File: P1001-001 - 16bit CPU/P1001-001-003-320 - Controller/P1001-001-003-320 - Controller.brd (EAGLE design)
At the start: 200 x 152 mm, 129 parts, among them IC10 74ALS00D, IC21 74LS138D, IC22 74LS138D, IC27 MEGA8535-A, IC3 74LS138D, IC4 74LS138D, IC5 74LS138D, J1 22-27-2041-04

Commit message: Check in the first try at soldering up the board
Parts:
- removed ABC_CLEAR, HALT_RESEDT_NEXTINS, PC_MAR_IR_IN, RAM_STACK_IN: (no value), jumper:JP2W
- removed B_OUT_PIMS, IN_C_D_X, STACK_C, STEP_PINS: (no value), jumper:JP4
- removed EXTRA6, INTERUPT_OUT: (no value), led:SFH482
- removed EXTRA_1_2_PINS, EXTRA_3_4_PINS, EXTRA_5_6_PINS, INTERUPTS, PC_INC_DEC, RAM_IMT_OUT: (no value), jumper:JP1
- removed IC10: 74ALS00D, 74xx-us:SO14
- removed J1: 22-27-2041-04, con-molex:6410-04
- removed PULL_DOWN: (no value), rcl:M0805
- removed R10: (no value), resistor-bourns:SO16
- added A11_A8, A15_A12, A7_A5, B11_B8, B15_B12, B7_B6, B_OUT_PINS, C11_C8, C15_C12, C7-C4, RAM_OUT_INTER: (no value), jumper:JP4
- added ALU_OUT, C_CLEAR_LED, FLAG_IN, INTER_DIS, INTER_EN, INTR_FLAG_OUT, INTR_REG_OUT: (no value), led:SFH482
- added IC1: 74ALS00D, 74xx-us:SO14
- added IC2: 74ALS02D, 74xx-us:SO14
- added IC6: 74ALS08D, 74xx-us:SO14
- added R6: (no value), resistor-bourns:SO16
- added STEP1_STEP3: (no value), jumper:JP2
- added STEP9: (no value), jumper:JP1
- moved PAUSE_INERUPT 102.0 mm to (133.0, 59.0)
- moved PLAY_INTERUPT 96.0 mm to (121.0, 59.0)
- moved X_OUT 83.2 mm to (13.0, 24.0)
- moved HALT 78.4 mm to (170.0, 60.0)
- moved EXTRA1 75.7 mm to (115.0, 48.0)
- moved EXTRA2 75.7 mm to (121.0, 48.0)
- moved EXTRA3 75.7 mm to (127.0, 48.0)
- moved EXTRA4 75.7 mm to (133.0, 48.0)
- moved EXTRA5 75.7 mm to (139.0, 48.0)
- moved RAM_OUT 74.6 mm to (41.0, 24.0)
- moved C_OUT 73.8 mm to (14.0, 36.0)
- moved NEXT_INS 72.7 mm to (158.0, 60.0)
- moved D_CLEAR_LED 69.6 mm to (77.0, 36.0)
- moved C_DEC 67.7 mm to (20.0, 36.0)
- moved C_INC 67.7 mm to (26.0, 36.0)
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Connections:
- new net FIRST_STEP: IC6.3, STEP9.1
- new net N$42: EXTRA5.K, R5.3
- new net N$50: EXTRA_OUT.3, EXTRA_OUT3.K, IC5.9
- new net N$56: EXTRA_OUT.4, EXTRA_OUT4.K, IC5.7
- new net N$57: EXTRA_OUT3.A, R2.9
- new net N$58: EXTRA_OUT4.A, R2.10
- new net N$59: R5.8, RESET.K
- new net N$60: HALT.K, R5.7
- new net N$61: IC2.4, IC6.2
- new net N$62: IC2.1, IC6.1
- new net N$63: NEXT_INS.K, R5.6
- net !CLEAR: now also IC1.1, IC1.2, IC1.6; no longer IC10.1, IC10.2, IC10.6
- net CLEAR: now also IC1.3; no longer IC10.3
- net DATAA10: now also A11_A8.3, A_CLEAR_LED.K; no longer EXTRA6.K, EXTRA_5_6_PINS.2
- net DATAA11: now also A11_A8.4, B_CLEAR_LED.K; no longer ABC_CLEAR.1, A_CLEAR_LED.K
- net DATAA12: now also A15_A12.1, C_CLEAR_LED.K; no longer ABC_CLEAR.2, B_CLEAR_LED.K
- net DATAA13: now also A15_A12.2; no longer ABC_CLEAR.3
- net DATAA14: now also A15_A12.3; no longer INTERUPTS.1
- net DATAA15: now also A15_A12.4; no longer INTERUPTS.2
- net DATAA5: now also A7_A5.2; no longer EXTRA_1_2_PINS.1
- net DATAA6: now also A7_A5.3; no longer EXTRA_1_2_PINS.2
- net DATAA7: now also A7_A5.4; no longer EXTRA_3_4_PINS.1
- net DATAA8: now also A11_A8.1; no longer EXTRA_3_4_PINS.2
- net DATAA9: now also A11_A8.2, EXTRA5.A; no longer EXTRA5.K, EXTRA_5_6_PINS.1
- net DATAB10: now also B11_B8.3; no longer PC_MAR_IR_IN.1
- net DATAB11: now also B11_B8.4; no longer PC_MAR_IR_IN.2
- net DATAB12: now also B15_B12.1; no longer PC_MAR_IR_IN.3
- net DATAB13: now also B15_B12.2; no longer RAM_STACK_IN.1
- net DATAB14: now also B15_B12.3; no longer RAM_STACK_IN.2
- net DATAB15: now also B15_B12.4; no longer RAM_STACK_IN.3
- net DATAB4: no longer PC_INC_DEC.2
- net DATAB6: now also B7_B6.3; no longer IN_C_D_X.1
- net DATAB7: now also B7_B6.4; no longer IN_C_D_X.2
- net DATAB8: now also B11_B8.1; no longer IN_C_D_X.3
- net DATAB9: now also B11_B8.2; no longer IN_C_D_X.4
- net DATAC10: now also C11_C8.3, FLAG_IN.A
- net DATAC11: now also C11_C8.4, INTER_EN.A
- net DATAC12: now also C15_C12.1, INTER_DIS.A
- net DATAC13: now also C15_C12.2, RESET.A; no longer HALT_RESEDT_NEXTINS.3, RESET.K
- net DATAC14: now also C15_C12.3, HALT.A; no longer HALT.K, HALT_RESEDT_NEXTINS.2
- net DATAC15: now also C15_C12.4, NEXT_INS.A; no longer HALT_RESEDT_NEXTINS.1, NEXT_INS.K
- net DATAC4: now also C7-C4.1, PC_DEC.A; no longer PC_DEC.K
- net DATAC5: now also C7-C4.2, PC_INC.A; no longer PC_INC.K, PC_INC_DEC.1
- net DATAC6: now also C7-C4.3, STACK_INC.A; no longer STACK_C.4, STACK_INC.K
- net DATAC7: now also C7-C4.4, STACK_DEC.A; no longer STACK_C.3, STACK_DEC.K
- net DATAC8: now also C11_C8.1, C_INC.A; no longer C_INC.K, STACK_C.2
- net DATAC9: now also C11_C8.2, C_DEC.A; no longer C_DEC.K, STACK_C.1
- net EXTERN_BUS0: no longer R10.1
- net EXTERN_BUS1: no longer R10.9
- net EXTERN_BUS10: no longer R10.6
- net EXTERN_BUS11: no longer R10.14
- net EXTERN_BUS12: no longer R10.7
- net EXTERN_BUS13: no longer R10.15
- net EXTERN_BUS14: no longer R10.8
- net EXTERN_BUS15: no longer PULL_DOWN.1
- net EXTERN_BUS2: no longer R10.2
- net EXTERN_BUS3: no longer R10.10
- net EXTERN_BUS4: no longer R10.3
- net EXTERN_BUS5: no longer R10.11
- net EXTERN_BUS6: no longer R10.4
- net EXTERN_BUS7: no longer R10.12
- net EXTERN_BUS8: no longer R10.5
- net EXTERN_BUS9: no longer R10.13
- net GND: now also IC1.7, IC2.7, IC6.7, R5.16, U$4.3, U$4.4; no longer IC10.7, J1.1, PULL_DOWN.2, R10.16
- net IN_BUS0: now also IC2.2, STEP9.2; no longer STEP_PINS.1
- net IN_BUS1: now also IC2.3, STEP1_STEP3.1; no longer STEP_PINS.2
- net IN_BUS2: now also IC2.5, STEP1_STEP3.2; no longer STEP_PINS.3
- net IN_BUS3: now also IC2.6, STEP1_STEP3.3; no longer STEP_PINS.4
- net N$1: now also IC1.4, IC1.5; no longer IC10.4, IC10.5
- net N$106: now also RAM_OUT_INTER.1; no longer RAM_IMT_OUT.1
- net N$107: now also INTR_REG_OUT.K, RAM_OUT_INTER.2; no longer INTERUPT_OUT.K, RAM_IMT_OUT.2
- net N$108: now also INTR_FLAG_OUT.K, RAM_OUT_INTER.3; no longer EXTRA_OUT.4, EXTRA_OUT1.K
- net N$109: now also ALU_OUT.K, RAM_OUT_INTER.4; no longer EXTRA_OUT.3, EXTRA_OUT2.K
- net N$110: now also EXTRA_OUT.1, EXTRA_OUT1.K; no longer EXTRA_OUT.2, EXTRA_OUT3.K
- net N$111: now also EXTRA_OUT.2, EXTRA_OUT2.K; no longer EXTRA_OUT.1, EXTRA_OUT4.K
- net N$113: now also EXTRA_OUT2.A; no longer EXTRA_OUT4.A
- net N$114: now also EXTRA_OUT1.A; no longer EXTRA_OUT3.A
- net N$115: now also ALU_OUT.A; no longer EXTRA_OUT2.A
- net N$116: now also INTR_FLAG_OUT.A; no longer EXTRA_OUT1.A
- net N$118: now also INTR_REG_OUT.A; no longer INTERUPT_OUT.A
- net N$16: now also PC_INC.K; no longer PC_INC.A
- net N$17: now also PC_DEC.K; no longer PC_DEC.A
- net N$18: now also R6.8, RAM_IN_H.A; no longer IR_IN.A, R5.3
- net N$19: now also R6.7, RAM_IN_L.A; no longer MAR_IN.A, R5.4
- net N$20: now also R6.6, STACK_IN.A; no longer PC_IN.A, R5.5
- net N$21: now also PC_IN.A, R6.5; no longer R5.6, STACK_IN.A
- net N$22: now also MAR_IN.A, R6.4; no longer R5.7, RAM_IN_L.A
- net N$23: now also IR_IN.A, R6.3; no longer R5.8, RAM_IN_H.A
- net N$24: now also INTER_DIS.K; no longer NEXT_INS.A
- net N$25: now also STACK_DEC.K; no longer STACK_DEC.A
- net N$26: now also C_INC.K; no longer C_INC.A
- net N$27: now also C_DEC.K; no longer C_DEC.A
- net N$28: now also FLAG_IN.K; no longer RESET.A
- net N$29: now also INTER_EN.K; no longer HALT.A
- net N$30: now also STACK_INC.K; no longer STACK_INC.A
- net N$43: now also IC1.8, U$4.1; no longer EXTRA5.A, R8.5
- net N$7: now also A_CLEAR_LED.A; no longer EXTRA6.A
- net N$79: now also B_OUT_PINS.1; no longer B_OUT_PIMS.1
- net N$8: now also C_CLEAR_LED.A; no longer B_CLEAR_LED.A
- net N$80: now also B_OUT_PINS.2; no longer B_OUT_PIMS.2
- net N$81: now also B_OUT_PINS.3; no longer B_OUT_PIMS.3
- net N$82: now also B_OUT_PINS.4; no longer B_OUT_PIMS.4
- net N$9: now also B_CLEAR_LED.A; no longer A_CLEAR_LED.A
- net NEXT_INS: now also IC1.10, IC1.9; no longer U$4.1
- net VCC: now also IC1.14, IC2.14, IC6.14, R6.16; no longer IC10.14, J1.2, R5.16, U$4.3, U$4.4
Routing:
- net N$75: track 170.0 -> 424.6 mm, vias 0 -> 1
- net N$88: track 177.0 -> 426.9 mm
- net N$50: track 0.00 -> 168.1 mm, vias 0 -> 6
- net DATAC12: track 0.00 -> 158.5 mm, vias 0 -> 7
- net N$56: track 0.00 -> 157.6 mm, vias 0 -> 8
- net N$57: track 0.00 -> 148.6 mm, vias 0 -> 9
- net N$1: track 33.8 -> 167.7 mm, vias 0 -> 2
- net DATAB4: track 231.4 -> 101.0 mm, vias 7 -> 0
- net CLEAR: track 20.0 -> 147.3 mm, vias 0 -> 1
- net DATAC4: track 41.1 -> 165.4 mm, vias 0 -> 5
- net DATAC11: track 0.00 -> 123.1 mm, vias 0 -> 8
- net DATAC10: track 0.00 -> 120.7 mm, vias 0 -> 3
- net N$19: track 188.5 -> 75.1 mm, vias 7 -> 2
- net N$58: track 0.00 -> 106.1 mm, vias 0 -> 7
- net DATAC8: track 101.1 -> 203.9 mm, vias 0 -> 7
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
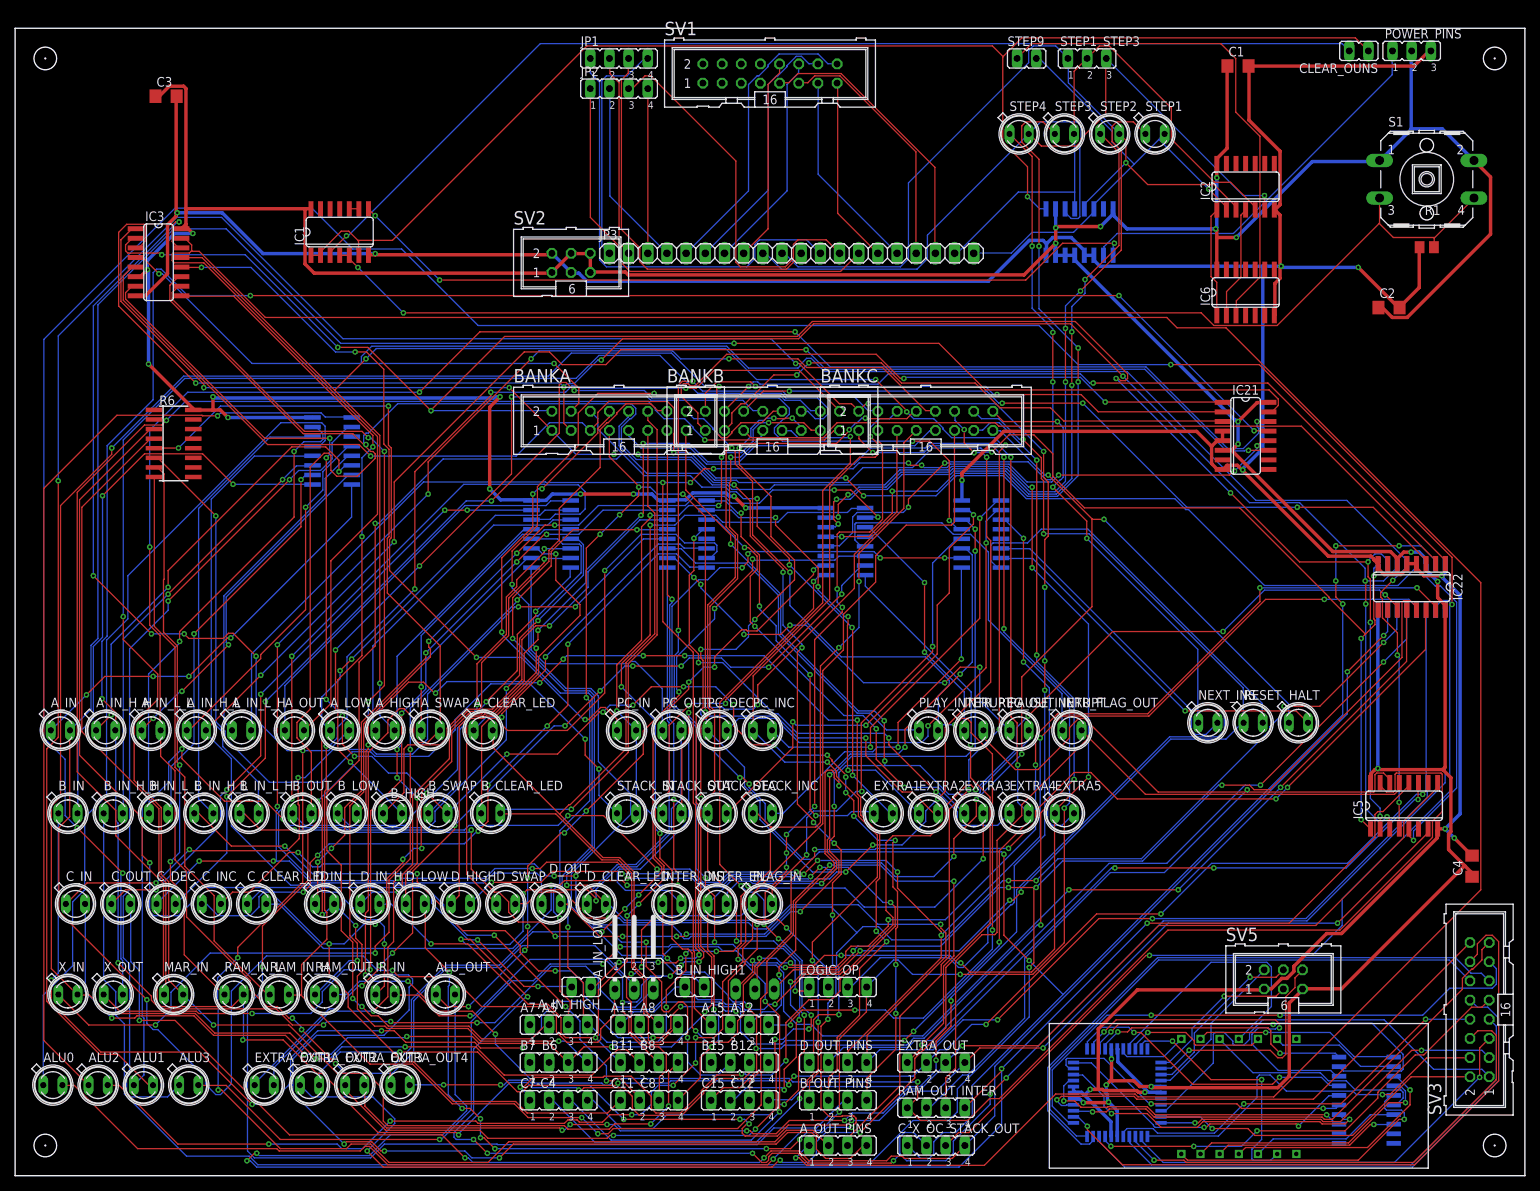
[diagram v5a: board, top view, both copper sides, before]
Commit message: ALU Register and controllker layout
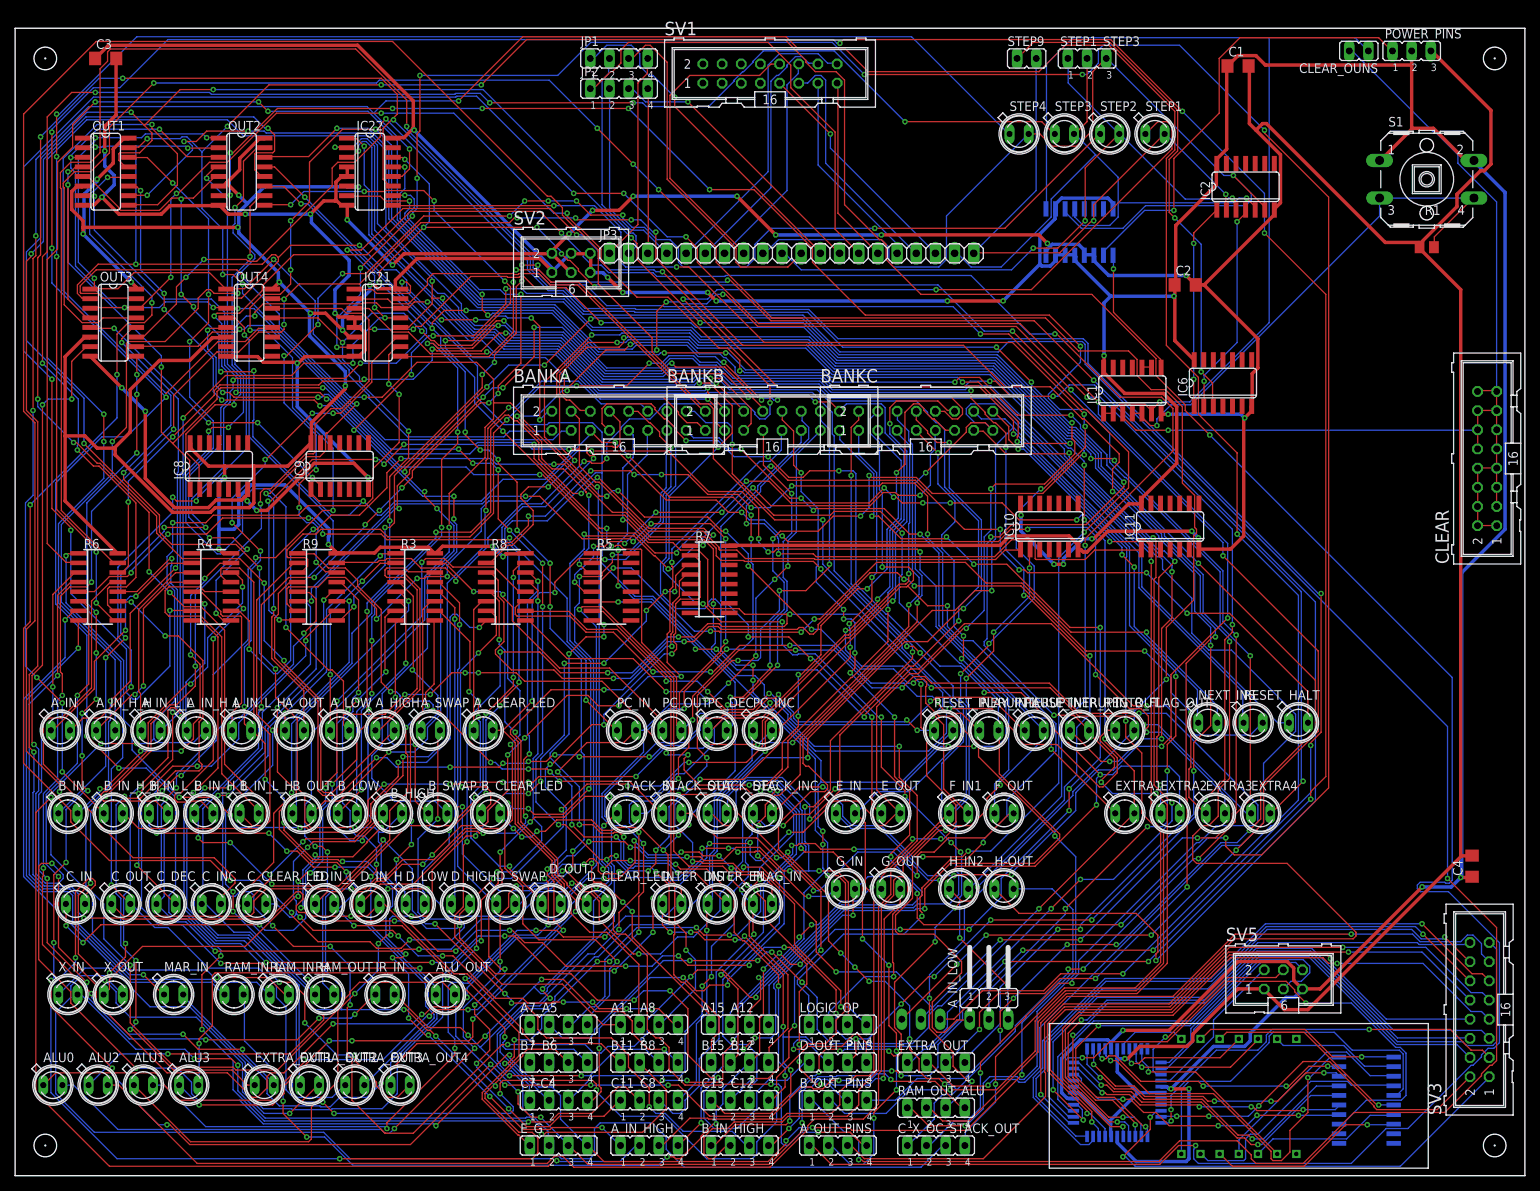
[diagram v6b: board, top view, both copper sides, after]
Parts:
- removed B_IN_HIGH1: (no value), jumper:JP1
- removed EXTRA5: (no value), led:SFH482
- removed IC3, IC4, IC5: 74LS138D, 74xx-us:SO16
- removed R2: (no value), resistor-bourns:SO16
- added B_IN_HIGH, E_G: (no value), jumper:JP4
- added CLEAR: (no value), con-harting-ml:ML16
- added E_IN, E_OUT, F_IN1, F_OUT, G_IN, G_OUT, H-OUT, H_IN2, RESET_INERUPT1: (no value), led:SFH482
- added IC10, IC11, IC8, IC9: 74ALS04D, 74xx-us:SO14
- added OUT1, OUT2, OUT3, OUT4: 74LS138D, 74xx-us:SO16
- added R7, R9: (no value), resistor-bourns:SO16
- A_IN_HIGH: device jumper:JP1 -> jumper:JP4
- moved IC22 148.6 mm to (47.0, 133.0), turned to 270 degrees
- moved IC21 116.0 mm to (48.0, 113.0)
- moved IC1 107.1 mm to (148.0, 104.0)
- moved R5 49.5 mm to (79.0, 78.0), flipped to the top
- moved A_IN_LOW 47.2 mm to (129.0, 22.0)
- moved EXTRA1 32.0 mm to (147.0, 48.0)
- moved EXTRA2 32.0 mm to (153.0, 48.0)
- moved EXTRA3 32.0 mm to (159.0, 48.0)
- moved EXTRA4 32.0 mm to (165.0, 48.0)
- moved C2 27.2 mm to (155.0, 118.0)
- moved R8 25.0 mm to (65.0, 78.0), flipped to the top
- moved R4 24.1 mm to (26.0, 78.0), flipped to the top
- moved A_IN_HIGH 22.8 mm to (84.0, 4.00), turned to 0 degrees
- moved B_IN_LOW1 22.4 mm to (120.0, 22.0)
- moved R6 21.5 mm to (11.0, 78.0)
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- renumbered RAM_OUT_INTER to RAM_OUT_ALU
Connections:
- removed net N$37: IC5.6
- removed net N$89 (its old number): C_X_OC_STACK_OUT.2, IC4.9, PC_OUT.K
- removed net N$90 (its old number): C_X_OC_STACK_OUT.1, IC4.7, STACK_OUT.K
- new net N$102: OUT3.15, RAM_OUT.K, RAM_OUT_ALU.1
- new net N$132: B_IN_L_L.K, R4.14
- new net N$135: B_IN.K, R4.15
- new net N$136: E_OUT.A, R9.6
- new net N$137: F_OUT.A, R9.7
- new net N$138: EXTRA_OUT3.A, R9.12
- new net N$139: EXTRA_OUT4.A, R9.13
- new net N$140: EXTRA_OUT.4, EXTRA_OUT1.K, OUT4.15
- new net N$141: EXTRA_OUT.3, EXTRA_OUT2.K, OUT4.14
- new net N$142: EXTRA_OUT.2, EXTRA_OUT3.K, OUT4.13
- new net N$143: EXTRA_OUT.1, EXTRA_OUT4.K, OUT4.12
- new net N$144: IC8.2, OUT2.4
- new net N$145: IC9.2, OUT3.5
- new net N$146: IC10.2, OUT4.4
- new net N$147: IC11.2, OUT4.5
- new net N$40: E_IN.A, R4.7
- new net N$53: F_IN1.K, R4.10
- new net N$65: A_IN_H_H.A, R4.4
- new net N$66: A_IN_L_L.A, R4.3
- new net N$71: A_IN.A, R4.2
- new net N$72: IC22.15
- new net N$74: B_IN_H_H.K, R4.13
- new net N$97: D_LOW.A, R3.11
- net CLEAR: now also CLEAR.1, CLEAR.10, CLEAR.11, CLEAR.12, CLEAR.13, CLEAR.14, CLEAR.15, CLEAR.16, CLEAR.2, CLEAR.3, CLEAR.4, CLEAR.5, CLEAR.6, CLEAR.7, CLEAR.8, CLEAR.9
- net DATAA0: now also OUT1.1, OUT2.1, OUT3.1, OUT4.1; no longer IC3.1, IC4.1, IC5.1
- net DATAA1: now also OUT1.2, OUT2.2, OUT3.2, OUT4.2; no longer IC3.2, IC4.2, IC5.2
- net DATAA10: now also B_CLEAR_LED.K; no longer A_CLEAR_LED.K
- net DATAA11: now also C_CLEAR_LED.K; no longer B_CLEAR_LED.K
- net DATAA12: now also D_CLEAR_LED.K; no longer C_CLEAR_LED.K
- net DATAA13: now also RESET_INERUPT1.K; no longer D_CLEAR_LED.K
- net DATAA2: now also OUT1.3, OUT2.3, OUT3.3, OUT4.3; no longer IC3.3, IC4.3, IC5.3
- net DATAA3: now also IC10.1, IC8.1, OUT1.4, OUT3.4; no longer IC3.4, IC4.4, IC5.4
- net DATAA4: now also IC11.1, IC9.1, OUT1.5, OUT2.5; no longer IC3.5, IC4.5, IC5.5
- net DATAA8: now also EXTRA4.A; no longer EXTRA4.K
- net DATAA9: now also A_CLEAR_LED.K; no longer EXTRA5.A
- net GND: now also IC10.7, IC11.7, IC8.7, IC9.7, OUT1.8, OUT2.8, OUT3.8, OUT4.8, R7.16; no longer IC3.8, IC4.8, IC5.8, R5.16
- net N$10: now also RESET_INERUPT1.A; no longer D_CLEAR_LED.A
- net N$100: now also D_SWAP.A, R3.13; no longer D_OUT.A, R3.14
- net N$101: now also R3.14, X_OUT.A; no longer D_LOW.A, R3.13
- net N$103: now also INTR_REG_OUT.K, OUT3.14, RAM_OUT_ALU.2; no longer D_SWAP.A, R3.11
- net N$104: now also INTR_FLAG_OUT.K, OUT3.13, RAM_OUT_ALU.3; no longer R3.10, X_OUT.A
- net N$105: now also ALU_OUT.K, OUT3.12, RAM_OUT_ALU.4; no longer PC_OUT.A, R3.9
- net N$106: now also E_G.1, E_OUT.K, OUT3.11; no longer IC5.15, RAM_OUT.K, RAM_OUT_ALU.1
- net N$107: now also E_G.2, F_OUT.K, OUT3.10; no longer IC5.14, INTR_REG_OUT.K, RAM_OUT_ALU.2
- net N$108: now also E_G.3, G_OUT.K, OUT3.9; no longer IC5.13, INTR_FLAG_OUT.K, RAM_OUT_ALU.3
- net N$109: now also E_G.4, H-OUT.K, OUT3.7; no longer ALU_OUT.K, IC5.12, RAM_OUT_ALU.4
- net N$110: now also R9.1, STACK_OUT.A; no longer EXTRA_OUT.1, EXTRA_OUT1.K, IC5.11
- net N$111: now also R9.2, RAM_OUT.A; no longer EXTRA_OUT.2, EXTRA_OUT2.K, IC5.10
- net N$112: now also G_OUT.A, R9.8; no longer R2.1, STACK_OUT.A
- net N$113: now also H-OUT.A, R9.9; no longer EXTRA_OUT2.A, R2.8
- net N$114: now also R9.10; no longer R2.7
- net N$115: now also EXTRA_OUT2.A, R9.11; no longer ALU_OUT.A, R2.6
- net N$116: now also INTR_REG_OUT.A, R9.3; no longer INTR_FLAG_OUT.A, R2.5
- net N$117: now also INTR_FLAG_OUT.A, R9.4; no longer R2.2, RAM_OUT.A
- net N$118: now also ALU_OUT.A, R9.5; no longer INTR_REG_OUT.A, R2.3
- net N$131: now also R9.15; no longer R2.15
- net N$133: now also R6.10; no longer R2.13
- net N$134: now also R6.9; no longer R2.12
- net N$16: now also PC_DEC.K, R6.2; no longer PC_INC.K, R5.1
- net N$17: now also PC_INC.K, R6.1; no longer PC_DEC.K, R5.2
- net N$24: now also R5.7; no longer R5.10
- net N$25: now also R6.15, STACK_INC.K; no longer R5.15, STACK_DEC.K
- net N$26: now also R6.14, STACK_DEC.K; no longer C_INC.K, R5.14
- net N$27: now also C_INC.K, R6.13; no longer C_DEC.K, R5.13
- net N$28: now also C_DEC.K, R6.12; no longer FLAG_IN.K, R5.12
- net N$29: now also R5.8; no longer R5.11
- net N$30: now also FLAG_IN.K, R6.11; no longer R5.9, STACK_INC.K
- net N$31: now also IC21.14; no longer IC21.15
- net N$32: now also IC21.13; no longer IC21.14
- net N$33: now also IC21.12; no longer IC21.13
- net N$34: now also IC21.11; no longer IC21.12
- net N$35: now also IC21.10; no longer IC21.11
- net N$36: now also A_IN_HIGH.3, E_IN.K, IC21.9; no longer A_IN.A, R4.8
- net N$38: now also A_IN_HIGH.4, G_IN.K, IC21.7; no longer A_IN_L_L.A, R4.7
- net N$39: now also G_IN.A, R4.8; no longer A_IN_H_H.A, R4.6
- net N$41: now also R4.6; no longer R4.4
- net N$42: now also D_CLEAR_LED.A, R8.5; no longer EXTRA5.K, R5.3
- net N$44: now also B_IN_HIGH.1, H_IN2.A, IC22.7; no longer B_IN.A, B_IN_LOW1.3, IC22.15
- net N$45: now also B_IN_HIGH.2, F_IN1.A, IC22.9; no longer B_IN_LOW1.2, B_IN_L_L.A, IC22.14
- net N$46: now also B_IN_HIGH.3, B_IN_H_L.A, IC22.10; no longer B_IN_H_H.A, B_IN_LOW1.1, IC22.13
- net N$47: now also B_IN_HIGH.4, IC22.11; no longer B_IN_HIGH1.2, IC22.12
- net N$48: now also B_IN_H_H.A, B_IN_LOW1.1, IC22.12; no longer B_IN_HIGH1.1, B_IN_H_L.A, IC22.11
- net N$49: now also B_IN_LOW1.2, B_IN_L_L.A, IC22.13; no longer B_IN.K, R4.9
- net N$5: now also EXTRA4.K, R5.3; no longer EXTRA4.A, R8.4
- net N$50: now also A_OUT.K, A_OUT_PINS.1, OUT1.15; no longer EXTRA_OUT.3, EXTRA_OUT3.K, IC5.9
- net N$51: now also B_IN.A, B_IN_LOW1.3, IC22.14; no longer B_IN_L_L.K, R4.10
- net N$52: now also H_IN2.K, R4.9; no longer B_IN_H_H.K, R4.11
- net N$54: now also R4.11; no longer R4.14
- net N$55: now also R9.14; no longer R2.14
- net N$56: now also A_LOW.K, A_OUT_PINS.2, OUT1.14; no longer EXTRA_OUT.4, EXTRA_OUT4.K, IC5.7
- net N$57: now also A_HIGH.K, A_OUT_PINS.3, OUT1.13; no longer EXTRA_OUT3.A, R2.9
- net N$58: now also A_OUT_PINS.4, A_SWAP.K, OUT1.12; no longer EXTRA_OUT4.A, R2.10
- net N$59: now also R5.6; no longer R5.8
- net N$60: now also R5.5; no longer R5.7
- net N$63: now also R5.4; no longer R5.6
- net N$67: now also R7.4; no longer R4.13
- net N$68: now also R7.3; no longer R4.15
- net N$69: now also R7.1; no longer R4.1
- net N$70: now also R7.2; no longer R4.2
- net N$75: now also B_OUT.K, B_OUT_PINS.1, OUT1.11; no longer A_OUT.K, A_OUT_PINS.1, IC3.15
- net N$76: now also B_LOW.K, B_OUT_PINS.2, OUT1.10; no longer A_LOW.K, A_OUT_PINS.2, IC3.14
- net N$77: now also B_HIGH.K, B_OUT_PINS.3, OUT1.9; no longer A_HIGH.K, A_OUT_PINS.3, IC3.13
- net N$78: now also B_OUT_PINS.4, B_SWAP.K, OUT1.7; no longer A_OUT_PINS.4, A_SWAP.K, IC3.12
- net N$79: now also C_OUT.K, D_OUT_PINS.4, OUT2.15; no longer B_OUT.K, B_OUT_PINS.1, IC3.11
- net N$80: now also D_OUT.K, D_OUT_PINS.3, OUT2.14; no longer B_LOW.K, B_OUT_PINS.2, IC3.10
- net N$81: now also D_LOW.K, D_OUT_PINS.2, OUT2.13; no longer B_HIGH.K, B_OUT_PINS.3, IC3.9
- net N$82: now also D_HIGH.K, D_OUT_PINS.1, OUT2.12; no longer B_OUT_PINS.4, B_SWAP.K, IC3.7
- net N$83: now also C_X_OC_STACK_OUT.4, D_SWAP.K, OUT2.11; no longer D_OUT.K, D_OUT_PINS.1, IC4.14
- net N$84: now also C_X_OC_STACK_OUT.3, OUT2.10, X_OUT.K; no longer C_OUT.K, C_X_OC_STACK_OUT.4, IC4.15
- net N$85: now also C_X_OC_STACK_OUT.2, OUT2.9, PC_OUT.K; no longer D_LOW.K, D_OUT_PINS.2, IC4.13
- net N$86: now also C_X_OC_STACK_OUT.1, OUT2.7, STACK_OUT.K; no longer D_HIGH.K, D_OUT_PINS.3, IC4.12
- net N$87: now also C_OUT.A, R3.9; no longer D_OUT_PINS.4, D_SWAP.K, IC4.11
- net N$88: now also D_OUT.A, R3.10; no longer C_X_OC_STACK_OUT.3, IC4.10, X_OUT.K
- net N$99: now also PC_OUT.A; no longer C_OUT.A
- net VCC: now also IC10.14, IC11.14, IC8.14, IC9.14, OUT1.16, OUT1.6, OUT2.16, OUT2.6, OUT3.16, OUT3.6, OUT4.16, OUT4.6, R9.16; no longer IC3.16, IC3.6, IC4.16, IC4.6, IC5.16, R2.16
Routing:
- net N$143: track 0.00 -> 518.5 mm, vias 0 -> 14
- net N$88: track 426.9 -> 47.0 mm, vias 5 -> 4
- net N$141: track 0.00 -> 378.8 mm, vias 0 -> 13
- net N$140: track 0.00 -> 376.4 mm, vias 0 -> 18
- net N$142: track 0.00 -> 375.1 mm, vias 0 -> 12
- net N$40: track 0.00 -> 369.2 mm, vias 0 -> 11
- net N$38: track 46.0 -> 381.7 mm, vias 3 -> 15
- net N$102: track 0.00 -> 330.9 mm, vias 0 -> 13
- net N$57: track 148.6 -> 470.7 mm, vias 9 -> 8
- net N$50: track 168.1 -> 487.7 mm, vias 6 -> 11
- net N$51: track 53.3 -> 359.6 mm, vias 2 -> 19
- net N$49: track 75.3 -> 358.5 mm, vias 2 -> 17
- net N$146: track 0.00 -> 280.0 mm, vias 0 -> 10
- net N$89 (its old number): track 275.3 -> 0.00 mm, vias 10 -> 0
- net N$25: track 61.2 -> 331.9 mm, vias 3 -> 6
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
